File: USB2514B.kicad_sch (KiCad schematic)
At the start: 44 parts, among them J1 USB_A, J2 USB_C_Receptacle_USB2.0_16P, J3 USB_A, J4 USB_A, J6 USB_A, U1 USB2514B_Bi, U10 USBLC6-2P6, U11 USBLC6-2P6, U2 USBLC6-2P6, U4 MCP1703Ax-330xxTT, U8 USBLC6-2P6, U9 USBLC6-2P6, X1 24MHz

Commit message: Ajout de toutes les pistes correspondant aux signaux, manque seulement les connexions à l'alimentation et la masse
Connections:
- net VOUT_PS1: no longer J1.1 (VBUS), J3.1 (VBUS), J6.1 (VBUS), U10.5 (VBUS), U11.5 (VBUS), U9.5 (VBUS)
- net D_USB4-: now reaches J3.2 (D-), U11.6 (I/O1)
- net D_USB4+: now reaches J3.3 (D+), U11.4 (I/O2)
- net D_USB1-: now reaches J4.2 (D-), U8.6 (I/O1)
- net D_USB1+: now reaches J4.3 (D+), U8.4 (I/O2)
- net D_USB3-: now reaches J1.2 (D-), U10.6 (I/O1)
- net D_USB3+: now reaches J1.3 (D+), U10.4 (I/O2)
- net D_USB2-: now reaches J6.2 (D-), U9.6 (I/O1)
- net D_USB2+: now reaches J6.3 (D+), U9.4 (I/O2)
- removed net EN: R11.2, R14.2, R17.2, R20.2, U1.12 (PRTPWR1/BC_EN1), U1.16 (PRTPWR2/BC_EN2), U1.18 (PRTPWR3/BC_EN3), U1.20 (PRTPWR4/BC_EN4)
- removed net FAULT: U1.13 (OCS_N1), U1.17 (OCS_N2), U1.19 (OCS_N3), U1.21 (OCS_N4)
- new net VOUT_PS2: J6.1 (VBUS), U9.5 (VBUS)
- new net VOUT_PS3: J1.1 (VBUS), U10.5 (VBUS)
- new net VOUT_PS4: J3.1 (VBUS), U11.5 (VBUS)
- new net power switches/EN: R11.2, U1.12 (PRTPWR1/BC_EN1)
- new net power switches/FAULT: U1.13 (OCS_N1)
- new net power switches1/EN: R14.2, U1.16 (PRTPWR2/BC_EN2)
- new net power switches1/FAULT: U1.17 (OCS_N2)
- new net power switches2/EN: R17.2, U1.18 (PRTPWR3/BC_EN3)
- new net power switches2/FAULT: U1.19 (OCS_N3)
- new net power switches3/EN: R20.2, U1.20 (PRTPWR4/BC_EN4)
- new net power switches3/FAULT: U1.21 (OCS_N4)
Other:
- sheet power switches ports: added EN, FAULT, VIN, VOUT; removed none
- sheet power switches1 ports: added EN, FAULT, VIN, VOUT; removed none
- sheet power switches2 ports: added EN, FAULT, VIN, VOUT; removed none
- sheet power switches3 ports: added EN, FAULT, VIN, VOUT; removed none
- moved on the sheet: J1, J3, J4, J6

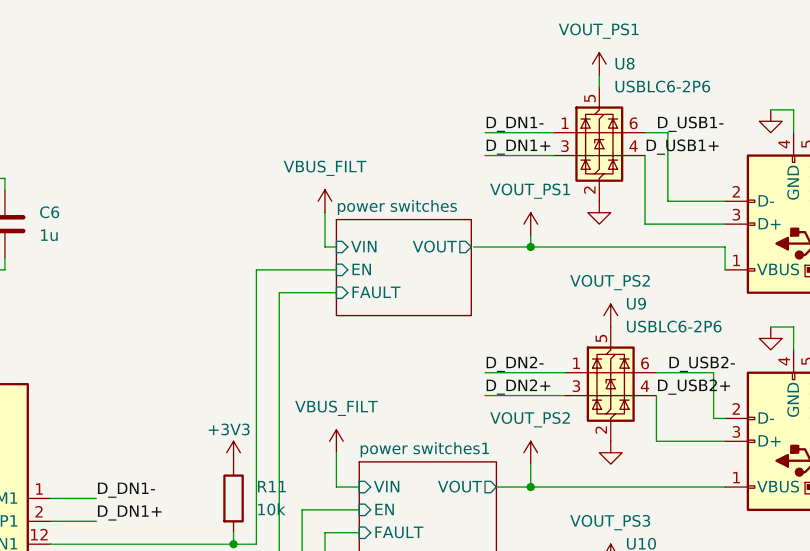
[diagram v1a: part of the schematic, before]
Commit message: Ajouter pistes alimentation 0.3mm pour 3.3V et 85mA max, connexion à la masse manquant
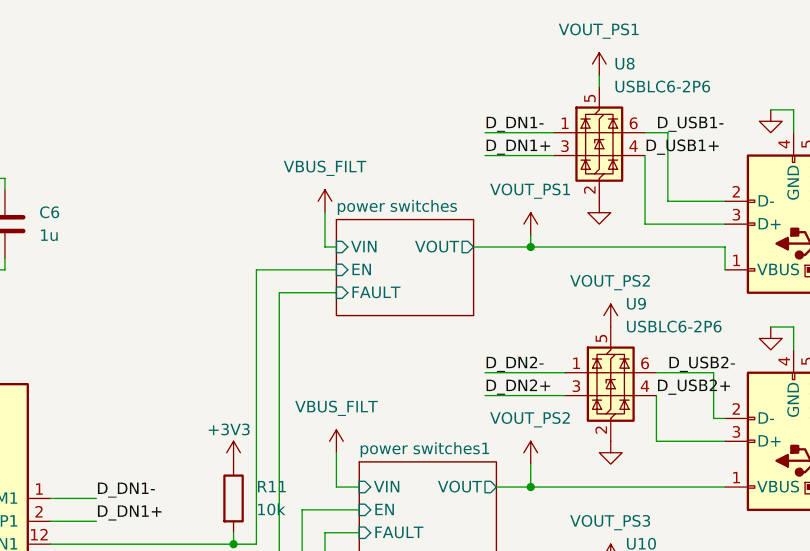
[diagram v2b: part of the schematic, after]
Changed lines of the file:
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@@
 	)
 	(junction
-		(at 247.65 45.72)
-		(diameter 0)
-		(color 0 0 0 0)
-	)
-	(junction
 		(at 163.83 55.88)
 		(diameter 0)
@@
 	)
 	(junction
+		(at 247.65 45.72)
+		(diameter 0)
+		(color 0 0 0 0)
+	)
+	(junction
 		(at 57.15 40.64)
 		(diameter 0)
@@
 	(wire
 		(pts
+			(xy 241.3 45.72) (xy 247.65 45.72)
+		)
+		(stroke
+			(width 0)
+			(type default)
+		)
+	)
+	(wire
+		(pts
 			(xy 276.86 111.76) (xy 274.32 111.76)
 		)
@@
 	(wire
 		(pts
-			(xy 241.3 45.72) (xy 247.65 45.72)
-		)
-		(stroke
-			(width 0)
-			(type default)
-		)
-	)
-	(wire
-		(pts
 			(xy 72.39 109.22) (xy 72.39 107.95)
 		)
@@
 	(sheet
 		(at 226.06 42.672)
-		(size 14.986 10.668)
+		(size 15.24 10.668)
 		(exclude_from_sim no)
 		(in_bom yes)
@@
 		)
 		(pin "VOUT" output
-			(at 241.046 45.72 0)
+			(at 241.3 45.72 0)
 			(effects
 				(font

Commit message: Generate GBR files and add symbols information for JLC-PCB PCBA purchase
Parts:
- C1, C11, C12, C2, C3, C4, C5, C6: Distrbutor Link 2 https://www.digikey.fr/fr/products/detail/murata-electronic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 -> (none); LCSC Part # (none) -> C363938
- C10, C9: LCSC Part # (none) -> C126625
- C14, C15: LCSC Part # (none) -> C1554
- C7, C8: Distribution Link https://www.mouser.fr/ProductDetail/KYOCERA-AVX/12065C104J4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 -> (none); Distributor Link 1 (none) -> https://www.mouser.fr/ProductDetail/KYOCERA-AVX/12065C104J4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; LCSC Part # (none) -> C6648471
- FB1: LCSC Part # (none) -> C14709
- J1, J3, J4, J6: Distributor Link 1 (none) -> https://www.mouser.fr/fr/ProductDetail/Amphenol-Commercial-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; LCSC Part # (none) -> C2345; Manufacturer (none) -> Amphenol Commercial Products; Manufacturer Part Number (none) -> 10502029K901A
- J2: Distributor Link 1 (none) -> https://www.mouser.fr/fr/ProductDetail/Same-Sky/UJ20-C-H-C-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; LCSC Part # (none) -> C36601498; Manufacturer (none) -> Same Sky; Manufacturer Part Number (none) -> UJ20-C-H-C-4-SMT-TR
- R1: LCSC Part # (none) -> C25741
- R11, R14, R17, R20, R3, R5, R6, R7, R8: Distributo Link 2 https://www.digikey.fr/fr/products/detail/yageo/RT0402WRD07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 -> (none); Distributor Link 2 (none) -> https://www.digikey.fr/fr/products/detail/yageo/RT0402WRD07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; LCSC Part # (none) -> C25531
- R2: Distributo Link 2 https://www.digikey.fr/fr/products/detail/yageo/RT0402WRD07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 -> (none); Distributor Link 2 (none) -> https://www.digikey.fr/fr/products/detail/yageo/RT0402WRD07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; LCSC Part # (none) -> C25741
- R4: LCSC Part # (none) -> C144798
- U1: Distributor Link 1 (none) -> https://www.mouser.fr/fr/ProductDetail/Microchip-Technology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; LCSC Part # (none) -> C58940; Manufacturer (none) -> Microchip Technology; Manufacturer Part Number (none) -> USB2514BI-AEZG-TR
- U10, U11, U8, U9: Distributor Link https://www.mouser.fr/ProductDetail/STMicroelectronics/USBL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 -> (none); Distributor Link 1 (none) -> https://www.mouser.fr/ProductDetail/STMicroelectronics/USBL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; LCSC Part # (none) -> C15999
- U2: Distributor Link https://www.mouser.fr/ProductDetail/STMicroelectronics/USBL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 -> (none); LCSC Part # (none) -> C15999
- U4: Distributor Link https://www.mouser.fr/ProductDetail/Microchip-Technology/MC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 -> (none); Distributor Link 1 (none) -> https://www.mouser.fr/ProductDetail/Microchip-Technology/MC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; LCSC Part # (none) -> C5236965
- X1: LCSC Part # (none) -> C6487089
